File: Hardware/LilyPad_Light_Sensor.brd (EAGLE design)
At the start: 20 x 20 mm, 9 parts, among them U1 TEMT6000

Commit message: Initial Commit
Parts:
- removed LIGHT+, LIGHT-, LIGHTS: SEWTAP6, LilyPad-Wearables:PETAL-SMALL-2SIDE
- removed LIGHT1, LIGHT2, LIGHT3: SEWTAP-NOHOLE2, LilyPad-Wearables:PETAL-NOHOLE-2SIDE
- removed R1: 10K, SparkFun:0402-RES
- removed U$2: LOGO-LPLP, LilyPad-Wearables:LOGO-LILYPAD
- removed U1: TEMT6000, SparkFun:TEMT6000-SEN
- added FRAME2: FRAME-LETTER, SparkFun-Aesthetics:CREATIVE_COMMONS
- added R24: 10k, SparkFun-Resistors:0603
- added SEWTAPLS+: PLUS, LilyPad-Wearables:PETAL-SMALL-2SIDE
- added SEWTAPLS-: MINUS, LilyPad-Wearables:PETAL-SMALL-2SIDE
- added SEWTAPLSOUT: OUT, LilyPad-Wearables:PETAL-SMALL-2SIDE
- added ST1, ST2, ST3: SEWTAP-NOHOLE_SM_NH, LilyPad-Wearables:PETAL-SMALL-NOHOLE
- added U$1: SPECIAL_INSTRUCTIONS-ORDERING, SparkFun-Aesthetics:ORDERING_INSTRUCTIONS
- added U$5: LILYLOGO_SHORT, newLilypadParts:LILYPAD-WEARABLES_LOGO-LILYPAD
- added U3: ALS-PT19, SparkFun-Sensors:ALS-PT19
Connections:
- removed net +: LIGHT+.1, U1.COLLECTOR
- removed net -: LIGHT-.1, R1.1
- removed net S: LIGHTS.1, R1.2, U1.EMITTER
- new net 3.3V: SEWTAPLS+.1, U3.C
- new net D2: R24.2, SEWTAPLSOUT.1, U3.E
- new net GND: R24.1, SEWTAPLS-.1
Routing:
- net 3.3V: track 0.00 -> 14.1 mm, vias 0 -> 1
- net D2: track 0.00 -> 13.1 mm, vias 0 -> 1
- net GND: track 0.00 -> 11.6 mm, vias 0 -> 1
- net S: track 10.2 -> 0.00 mm
- net +: track 7.34 -> 0.00 mm
- net -: track 5.26 -> 0.00 mm
- net SEWTAP+1: track 0.00 -> 2.02 mm
- added copper zone on layer 1, net N$45
- added copper zone on layer 16, net N$46
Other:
- board size 20 x 20 mm -> 19.5 x 19.5 mm
- board text added: "Finishing: Lead-free HASL"
- board text added: "Light Sensor"
- board text added: "LilyPad concept and shapes by: L. Buechley and N. Seidle"
- board text added: "Marshal Taylor"
- board text added: "Marshall Taylor"
- board text added: "PCB thickness: 31 mil / 0.8mm"
- board text added: "Plated holes: 0.0866"
- board text added: "Revised by: Elias Santistevan"
- board text added: "Solder mask color: Purple (Lilypad)"
- board text added: "U3"
- board text added: "Unplated holes: 0.02"

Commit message: Cleaned up some things
Read for review
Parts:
- moved ST3 12.2 mm to (3.05, 13.5), turned to 240 degrees
- moved SEWTAPLSOUT 11.7 mm to (9.65, 17.3), turned to 180 degrees
- moved SEWTAPLS+ 11.3 mm to (3.05, 5.84), turned to 300 degrees
- moved ST2 10.4 mm to (16.3, 13.5), turned to 120 degrees
- moved ST1 9.94 mm to (9.65, 2.03), turned to 0 degrees
- moved SEWTAPLS- 9.40 mm to (16.3, 5.84), turned to 60 degrees
- moved R24 2.67 mm to (12.2, 9.65), turned to 90 degrees
- moved U3 1.40 mm to (9.65, 9.65), turned to 90 degrees
- moved U$5 1.15 mm to (9.65, 9.29), turned to 0 degrees
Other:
- board size 19.5 x 19.5 mm -> 19.3 x 19.3 mm
- board text added: "Inches"
- board text added: "v01"

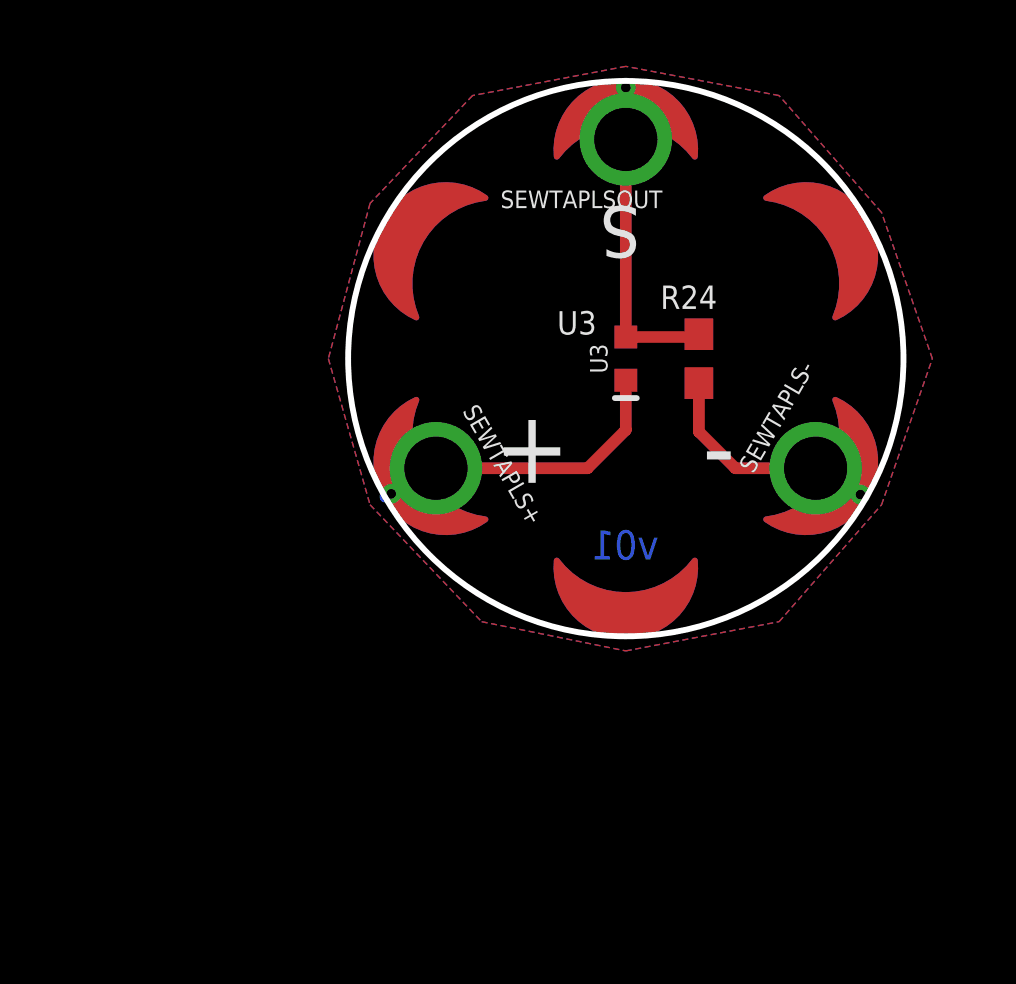
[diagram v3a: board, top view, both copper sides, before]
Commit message: Fiducials, VCC Range added
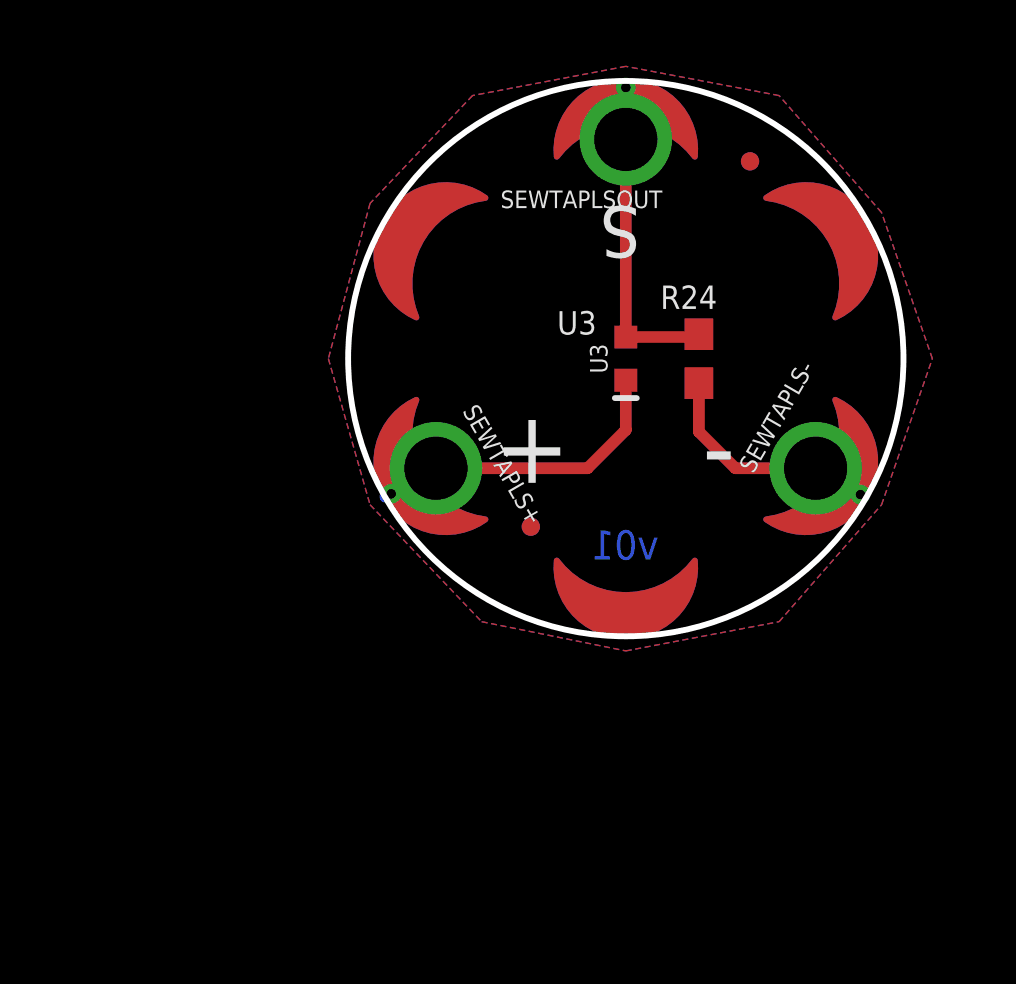
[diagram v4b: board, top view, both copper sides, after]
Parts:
- added FD1, FD2, FD3, FD4: FIDUCIALUFIDUCIAL, SparkFun-Aesthetics:FIDUCIAL-MICRO
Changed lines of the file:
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@@
 <element name="U$5" library="newLilypadParts" package="LILYPAD-WEARABLES_LOGO-LILYPAD" value="LILYLOGO_SHORT" x="9.652" y="9.2948125" rot="MR0"/>
 <element name="U$1" library="SparkFun-Aesthetics" package="ORDERING_INSTRUCTIONS" value="SPECIAL_INSTRUCTIONS-ORDERING" x="-6.35" y="-26.67"/>
+<element name="FD1" library="SparkFun-Aesthetics" package="FIDUCIAL-MICRO" value="FIDUCIALUFIDUCIAL" x="13.97" y="16.51"/>
+<element name="FD2" library="SparkFun-Aesthetics" package="FIDUCIAL-MICRO" value="FIDUCIALUFIDUCIAL" x="6.35" y="3.81"/>
+<element name="FD3" library="SparkFun-Aesthetics" package="FIDUCIAL-MICRO" value="FIDUCIALUFIDUCIAL" x="6.35" y="3.81" rot="MR0"/>
+<element name="FD4" library="SparkFun-Aesthetics" package="FIDUCIAL-MICRO" value="FIDUCIALUFIDUCIAL" x="13.97" y="16.51" rot="MR0"/>
 </elements>
 <signals>

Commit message: Fixes from double check
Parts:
- added LOGO1: OSHW-LOGOMINI, SparkFun-Aesthetics:OSHW-LOGO-MINI
- added LOGO2: SFE_LOGO_FLAME.1_INCH, SparkFun-Aesthetics:SFE_LOGO_FLAME_.1
- renumbered R24 to R1, U3 to U1
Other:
- board text added: "v14"
- board text removed: "v01"
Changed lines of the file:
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@@
 <board>
 <plain>
-<text x="52.07" y="-9.68375" size="1.778" layer="51" font="vector" align="top-left">Marshall Taylor</text>
+<text x="-52.07" y="-9.68375" size="1.778" layer="52" font="vector" rot="MR0" align="top-left">Marshall Taylor</text>
 <text x="9.45825" y="14.942" size="1.778" layer="21" ratio="15" rot="SR180" align="bottom-center">S</text>
 <text x="12.319" y="5.334" size="2.54" layer="21" ratio="15" rot="SR0">-</text>
@@
 <wire x1="18.70075" y1="4.41325" x2="18.2245" y2="4.73075" width="0.4064" layer="30"/>
 <wire x1="9.6302625" y1="19.566965625" x2="9.637509375" y2="19.9424375" width="0.4064" layer="30"/>
-<text x="-3.81" y="-36.83" size="1.778" layer="51" align="top-left">PCB thickness: 31 mil / 0.8mm </text>
-<text x="-6.35" y="-19.84375" size="1.778" layer="51" font="vector" align="top-left">LilyPad concept and shapes by:  L. Buechley and N. Seidle</text>
-<text x="-3.81" y="-40.64" size="1.778" layer="51" align="top-left">Solder mask color: Purple (Lilypad)</text>
-<text x="-3.81" y="-44.45" size="1.778" layer="51" align="top-left">Finishing: Lead-free HASL</text>
+<text x="3.81" y="-36.83" size="1.778" layer="52" rot="MR0" align="top-left">PCB thickness: 31 mil / 0.8mm </text>
+<text x="6.35" y="-19.84375" size="1.778" layer="52" font="vector" rot="MR0" align="top-left">LilyPad concept and shapes by:  L. Buechley and N. Seidle</text>
+<text x="3.81" y="-40.64" size="1.778" layer="52" rot="MR0" align="top-left">Solder mask color: Purple (Lilypad)</text>
+<text x="3.81" y="-44.45" size="1.778" layer="52" rot="MR0" align="top-left">Finishing: Lead-free HASL</text>
 <text x="15.8035625" y="11.9141875" size="1.27" layer="22" font="vector" ratio="15" rot="MR0">Light Sensor</text>
 <wire x1="18.8171375" y1="4.3538" x2="16.251121875" y2="5.842" width="0.4064" layer="29"/>
 <wire x1="18.8171375" y1="4.3538" x2="16.251121875" y2="5.842" width="0.4064" layer="30"/>
-<circle x="9.652" y="9.652" radius="9.67646875" width="0.4064" layer="51"/>
+<circle x="-9.652" y="9.652" radius="9.67646875" width="0.4064" layer="52"/>
 <polygon width="0.2032" layer="42">
 <vertex x="6.731" y="14.711325" curve="-180"/>
@@
 <vertex x="14.9804125" y="18.796"/>
 </polygon>
-<text x="-3.81" y="-48.26" size="1.778" layer="51" align="top-left">Unplated holes:
+<text x="3.81" y="-48.26" size="1.778" layer="52" rot="MR0" align="top-left">Unplated holes:
 0.02
 </text>
-<text x="22.86" y="-48.26" size="1.778" layer="51" align="top-left">Plated holes:
+<text x="-22.86" y="-48.26" size="1.778" layer="52" rot="MR0" align="top-left">Plated holes:
 0.0866
 </text>
@@
 <vertex x="9.652" y="17.852"/>
 </polygon>
-<text x="16.51" y="-19.05" size="1.778" layer="51" font="vector">Revised by: Elias Santistevan</text>
-<text x="35.56" y="-16.51" size="1.778" layer="51" font="vector">Marshal Taylor</text>
+<text x="-16.51" y="-19.05" size="1.778" layer="52" font="vector" rot="MR0">Revised by: Elias Santistevan</text>
+<text x="-35.56" y="-16.51" size="1.778" layer="52" font="vector" rot="MR0">Marshal Taylor</text>
 <circle x="9.652" y="9.652" radius="9.652" width="0.2032" layer="47"/>
 <text x="6.604" y="23.622" size="1.778" layer="47" font="vector" ratio="15">Inches</text>
-<text x="10.795" y="2.667" size="1.016" layer="16" font="vector" ratio="15" rot="MR0">v01</text>
+<text x="10.795" y="2.667" size="1.016" layer="16" font="vector" ratio="15" rot="MR0">v14</text>
 <circle x="9.652" y="9.652" radius="9.652" width="0.2032" layer="20"/>
 <dimension x1="0" y1="9.652" x2="19.304" y2="9.652" x3="9.652" y3="26.289" textsize="1.778" textratio="15" layer="47" dtype="diameter" unit="inch"/>
+<text x="-173.99" y="-33.02" size="1.778" layer="52" rot="MR0" align="top-left">PCB thickness: 31 mil / 0.8mm </text>
+<text x="-171.45" y="-16.03375" size="1.778" layer="52" font="vector" rot="MR0" align="top-left">LilyPad concept and shapes by:  L. Buechley and N. Seidle</text>
+<text x="-173.99" y="-36.83" size="1.778" layer="52" rot="MR0" align="top-left">Solder mask color: Purple (Lilypad)</text>
+<text x="-173.99" y="-40.64" size="1.778" layer="52" rot="MR0" align="top-left">Finishing: Lead-free HASL</text>
+<text x="-173.99" y="-44.45" size="1.778" layer="52" rot="MR0" align="top-left">Unplated holes:
+0.02
+</text>
+<text x="-200.66" y="-44.45" size="1.778" layer="52" rot="MR0" align="top-left">Plated holes:
+0.0866
+</text>
+<text x="-194.31" y="-15.24" size="1.778" layer="52" font="vector" rot="MR0">Revised by: Elias Santistevan</text>
+<text x="-3.81" y="-36.83" size="1.778" layer="51" align="top-left">PCB thickness: 31 mil / 0.8mm </text>
+<text x="-3.81" y="-40.64" size="1.778" layer="51" align="top-left">Solder mask color: Purple (Lilypad)</text>
+<text x="-3.81" y="-44.45" size="1.778" layer="51" align="top-left">Finishing: Lead-free HASL</text>
+<text x="-3.81" y="-48.26" size="1.778" layer="51" align="top-left">Unplated holes:
+0.02
+</text>
+<text x="22.86" y="-48.26" size="1.778" layer="51" align="top-left">Plated holes:
+0.0866
+</text>
+<text x="-5.08" y="-21.11375" size="1.778" layer="51" font="vector" align="top-left">LilyPad concept and shapes by:  L. Buechley and N. Seidle</text>
+<text x="16.51" y="-19.05" size="1.778" layer="51" font="vector">Revised by: Elias Santistevan</text>
+<text x="35.56" y="-16.51" size="1.778" layer="51" font="vector">Marshall Taylor</text>
 </plain>
 <attributes>
@@
 <element name="SEWTAPLS+" library="LilyPad-Wearables" package="PETAL-SMALL-2SIDE" value="PLUS" x="3.052878125" y="5.842" rot="R300"/>
 <element name="SEWTAPLSOUT" library="LilyPad-Wearables" package="PETAL-SMALL-2SIDE" value="OUT" x="9.652" y="17.272" rot="R180"/>
-<element name="R24" library="SparkFun-Resistors" package="0603" value="10k" x="12.192" y="9.652" smashed="yes" rot="R90">
+<element name="R1" library="SparkFun-Resistors" package="0603" value="10k" x="12.192" y="9.652" smashed="yes" rot="R90">
 <attribute name="PROD_ID" value="RES-00824" x="23.622" y="9.652" size="0.70611875" layer="27" font="vector" rot="R90" display="off"/>
 <attribute name="NAME" x="12.827" y="12.192" size="0.8128" layer="25" font="vector" rot="R180"/>
 <attribute name="VALUE" value="10k" x="13.335" y="8.636" size="0.4064" layer="27" font="vector" rot="R90"/>
 </element>
-<element name="U3" library="SparkFun-Sensors" package="ALS-PT19" value="ALS-PT19" x="9.652" y="9.652" rot="R90">
+<element name="U1" library="SparkFun-Sensors" package="ALS-PT19" value="ALS-PT19" x="9.652" y="9.652" rot="R90">
 <attribute name="PROD_ID" value="IC-11836" x="24.257" y="6.477" size="0.70611875" layer="27" font="vector" rot="R90" display="off"/>
 <attribute name="SF_ID" value="SEN-12566" x="9.652" y="9.652" size="1.778" layer="27" rot="R90" display="off"/>
@@
 <element name="FD3" library="SparkFun-Aesthetics" package="FIDUCIAL-MICRO" value="FIDUCIALUFIDUCIAL" x="6.35" y="3.81" rot="MR0"/>
 <element name="FD4" library="SparkFun-Aesthetics" package="FIDUCIAL-MICRO" value="FIDUCIALUFIDUCIAL" x="13.97" y="16.51" rot="MR0"/>
+<element name="LOGO1" library="SparkFun-Aesthetics" package="OSHW-LOGO-MINI" value="OSHW-LOGOMINI" x="8.509" y="4.572" rot="MR0"/>
+<element name="LOGO2" library="SparkFun-Aesthetics" package="SFE_LOGO_FLAME_.1" value="SFE_LOGO_FLAME.1_INCH" x="12.192" y="2.921" rot="MR0"/>
 </elements>
 <signals>
 <signal name="GND">
 <contactref element="SEWTAPLS-" pad="1"/>
-<contactref element="R24" pad="1"/>
+<contactref element="R1" pad="1"/>
 <wire x1="17.8011375" y1="4.9888" x2="16.251121875" y2="5.842" width="0.4064" layer="1"/>
 <wire x1="12.192" y1="7.112" x2="12.192" y2="8.802" width="0.4064" layer="1"/>
@@
 <signal name="3.3V">
 <contactref element="SEWTAPLS+" pad="1"/>
-<contactref element="U3" pad="C"/>
+<contactref element="U1" pad="C"/>
 <wire x1="9.652" y1="8.902" x2="9.652" y2="7.172" width="0.4064" layer="1"/>
 <wire x1="9.652" y1="7.172" x2="8.322" y2="5.842" width="0.4064" layer="1"/>
@@
 <signal name="D2">
 <contactref element="SEWTAPLSOUT" pad="1"/>
-<contactref element="R24" pad="2"/>
-<contactref element="U3" pad="E"/>
+<contactref element="R1" pad="2"/>
+<contactref element="U1" pad="E"/>
 <wire x1="9.652" y1="10.402" x2="12.192" y2="10.402" width="0.4064" layer="1"/>
 <wire x1="12.192" y1="10.402" x2="12.192" y2="10.502" width="0.4064" layer="1"/>

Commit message: Double Check changes!
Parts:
- moved LOGO1 7.55 mm to (2.92, 9.65)
- moved LOGO2 7.10 mm to (17.0, 8.13)
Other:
- board text added: "v20"
- board text removed: "v14"
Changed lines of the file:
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@@
 <circle x="9.652" y="9.652" radius="9.652" width="0.2032" layer="47"/>
 <text x="6.604" y="23.622" size="1.778" layer="47" font="vector" ratio="15">Inches</text>
-<text x="10.795" y="2.667" size="1.016" layer="16" font="vector" ratio="15" rot="MR0">v14</text>
+<text x="10.795" y="2.667" size="1.016" layer="16" font="vector" ratio="15" rot="MR0">v20</text>
 <circle x="9.652" y="9.652" radius="9.652" width="0.2032" layer="20"/>
 <dimension x1="0" y1="9.652" x2="19.304" y2="9.652" x3="9.652" y3="26.289" textsize="1.778" textratio="15" layer="47" dtype="diameter" unit="inch"/>
@@
 </text>
 <text x="-194.31" y="-15.24" size="1.778" layer="52" font="vector" rot="MR0">Revised by: Elias Santistevan</text>
+<text x="3.81" y="-36.83" size="1.778" layer="52" rot="MR0" align="top-left">PCB thickness: 31 mil / 0.8mm </text>
+<text x="3.81" y="-40.64" size="1.778" layer="52" rot="MR0" align="top-left">Solder mask color: Purple (Lilypad)</text>
+<text x="3.81" y="-44.45" size="1.778" layer="52" rot="MR0" align="top-left">Finishing: Lead-free HASL</text>
+<text x="3.81" y="-48.26" size="1.778" layer="52" rot="MR0" align="top-left">Unplated holes:
+0.02
+</text>
+<text x="-22.86" y="-48.26" size="1.778" layer="52" rot="MR0" align="top-left">Plated holes:
+0.0866
+</text>
+<text x="5.08" y="-21.11375" size="1.778" layer="52" font="vector" rot="MR0" align="top-left">LilyPad concept and shapes by:  L. Buechley and N. Seidle</text>
+<text x="-16.51" y="-19.05" size="1.778" layer="52" font="vector" rot="MR0">Revised by: Elias Santistevan</text>
+<text x="-35.56" y="-16.51" size="1.778" layer="52" font="vector" rot="MR0">Marshall Taylor</text>
+<text x="-142.24" y="-39.37" size="1.778" layer="52" rot="MR0" align="top-left">PCB thickness: 31 mil / 0.8mm </text>
+<text x="-142.24" y="-43.18" size="1.778" layer="52" rot="MR0" align="top-left">Solder mask color: Purple (Lilypad)</text>
+<text x="-142.24" y="-46.99" size="1.778" layer="52" rot="MR0" align="top-left">Finishing: Lead-free HASL</text>
+<text x="-142.24" y="-50.8" size="1.778" layer="52" rot="MR0" align="top-left">Unplated holes:
+0.02
+</text>
+<text x="-168.91" y="-50.8" size="1.778" layer="52" rot="MR0" align="top-left">Plated holes:
+0.0866
+</text>
+<text x="-140.97" y="-23.65375" size="1.778" layer="52" font="vector" rot="MR0" align="top-left">LilyPad concept and shapes by:  L. Buechley and N. Seidle</text>
+<text x="-162.56" y="-21.59" size="1.778" layer="52" font="vector" rot="MR0">Revised by: Elias Santistevan</text>
+<text x="-181.61" y="-19.05" size="1.778" layer="52" font="vector" rot="MR0">Marshall Taylor</text>
 <text x="-3.81" y="-36.83" size="1.778" layer="51" align="top-left">PCB thickness: 31 mil / 0.8mm </text>
 <text x="-3.81" y="-40.64" size="1.778" layer="51" align="top-left">Solder mask color: Purple (Lilypad)</text>
@@
 <element name="FD3" library="SparkFun-Aesthetics" package="FIDUCIAL-MICRO" value="FIDUCIALUFIDUCIAL" x="6.35" y="3.81" rot="MR0"/>
 <element name="FD4" library="SparkFun-Aesthetics" package="FIDUCIAL-MICRO" value="FIDUCIALUFIDUCIAL" x="13.97" y="16.51" rot="MR0"/>
-<element name="LOGO1" library="SparkFun-Aesthetics" package="OSHW-LOGO-MINI" value="OSHW-LOGOMINI" x="8.509" y="4.572" rot="MR0"/>
-<element name="LOGO2" library="SparkFun-Aesthetics" package="SFE_LOGO_FLAME_.1" value="SFE_LOGO_FLAME.1_INCH" x="12.192" y="2.921" rot="MR0"/>
+<element name="LOGO1" library="SparkFun-Aesthetics" package="OSHW-LOGO-MINI" value="OSHW-LOGOMINI" x="2.921" y="9.652" rot="MR0"/>
+<element name="LOGO2" library="SparkFun-Aesthetics" package="SFE_LOGO_FLAME_.1" value="SFE_LOGO_FLAME.1_INCH" x="17.018" y="8.128" rot="MR0"/>
 </elements>
 <signals>
